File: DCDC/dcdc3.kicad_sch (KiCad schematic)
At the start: 29 parts, among them IC1 LM5145RGYR, J1 Vin, J2 GND, J3 Vout, J4 GND, M1 30V 60A, M2 30V 35A

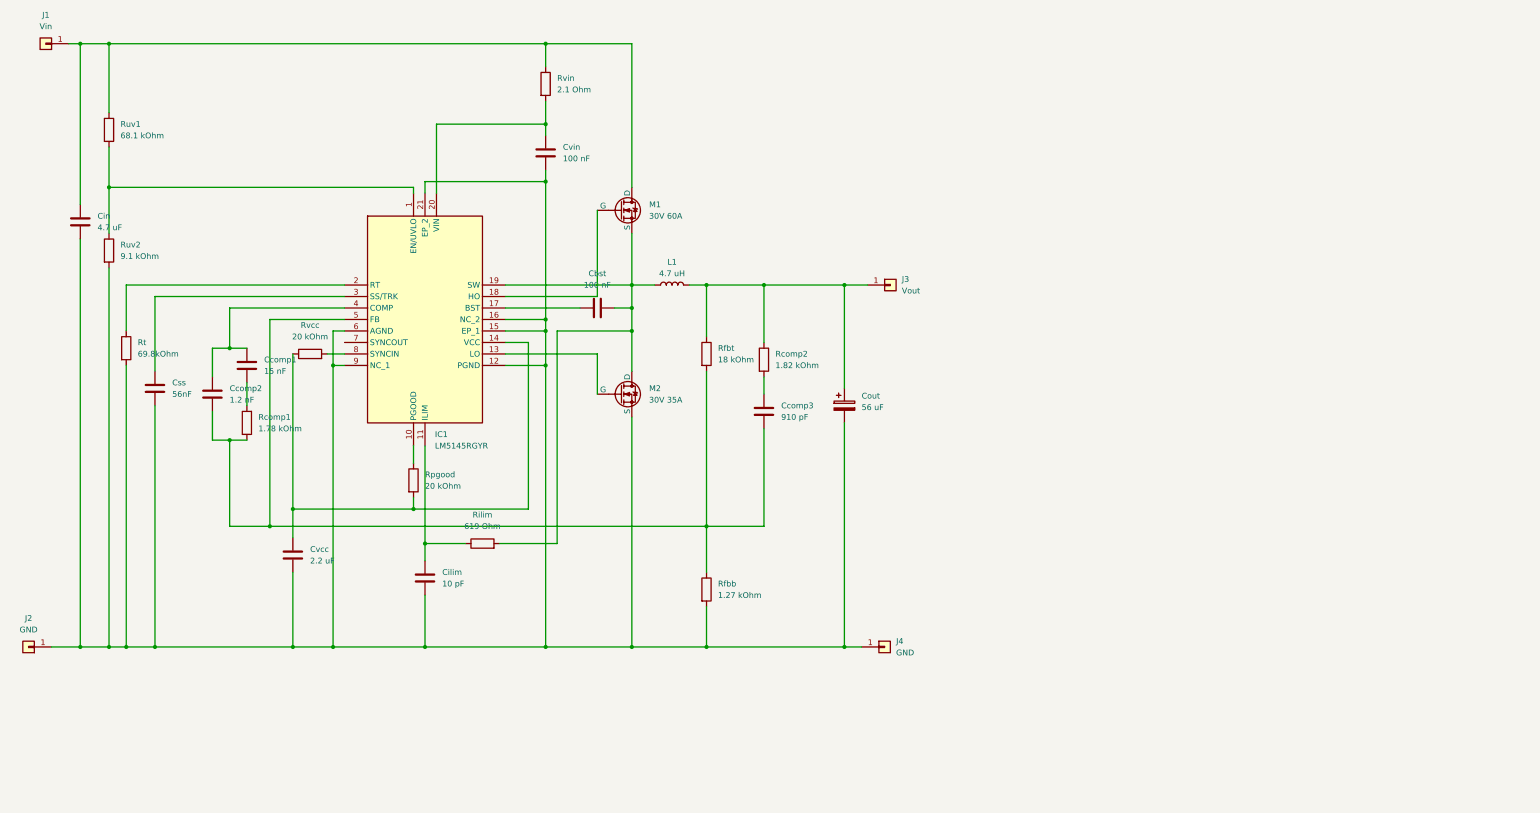
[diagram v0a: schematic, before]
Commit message: redesign of voltage regulator
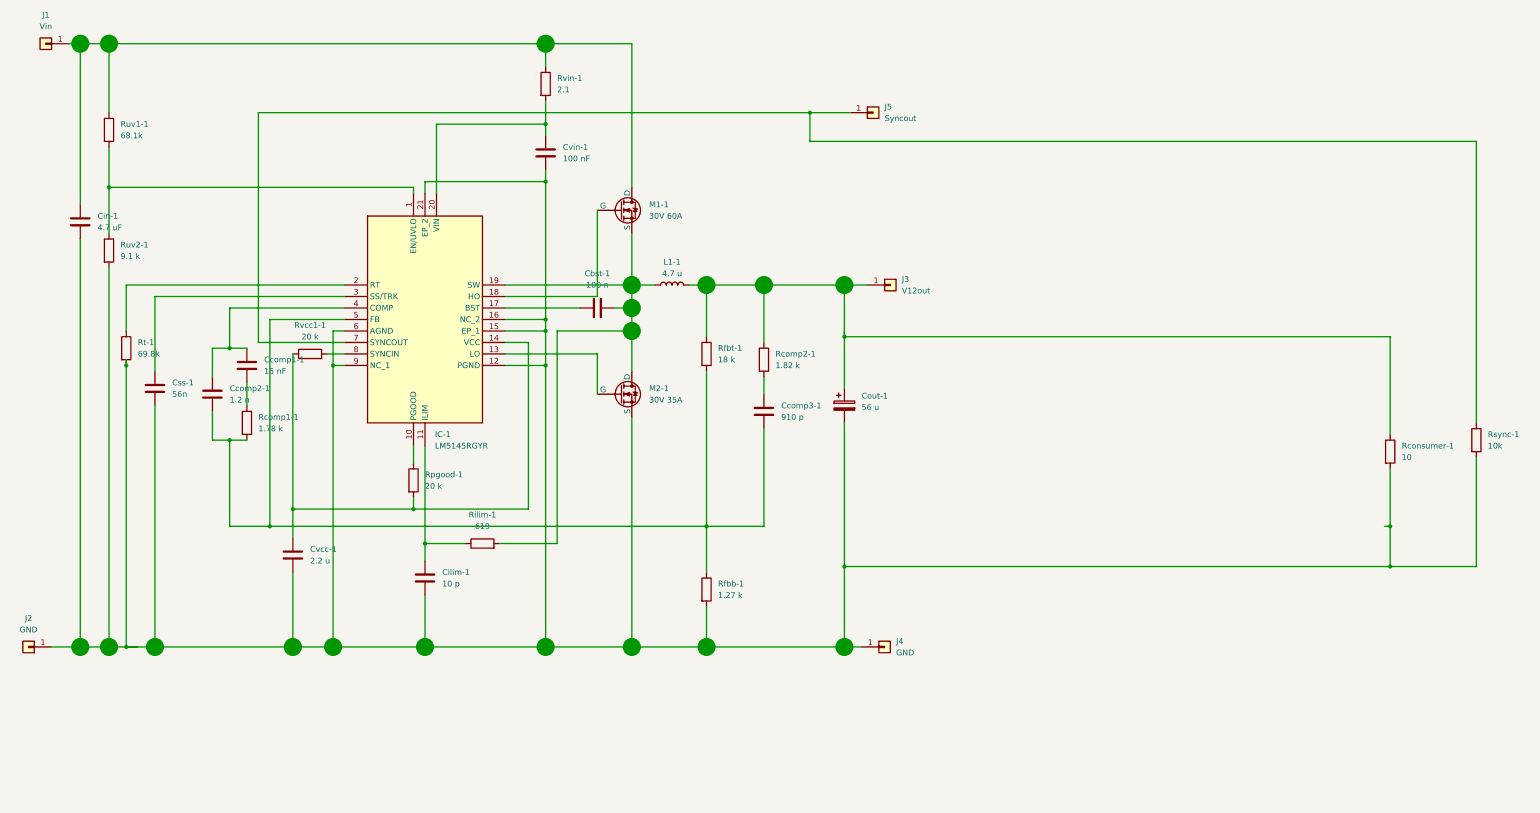
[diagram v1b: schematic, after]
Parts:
- added J5: Syncout, Connector_Pin:Pin_D1.4mm_L8.5mm_W2.8mm_FlatFork, symbol Connector_Generic:Conn_01x01
- added Rconsumer-1: 10, symbol Device:R
- added Rsync-1: 10k, symbol Device:R
- Cbst-1: renamed from Cbst; value 100 nF -> 100 n; footprint (none) -> Capacitor_SMD:C_0603_1608Metric; Manufacturer_Part_Number (none) -> GRM188R61E104KA01D
- Ccomp1-1: renamed from Ccomp1; footprint (none) -> Capacitor_SMD:C_0402_1005Metric; Manufacturer_Part_Number (none) -> GRM155R71C153KA01D
- Ccomp2-1: renamed from Ccomp2; value 1.2 nF -> 1.2 n; footprint (none) -> Capacitor_SMD:C_0402_1005Metric; Manufacturer_Part_Number (none) -> GRM155R71H122KA01D
- Ccomp3-1: renamed from Ccomp3; value 910 pF -> 910 p; footprint (none) -> Capacitor_SMD:C_0402_1005Metric; Manufacturer_Part_Number (none) -> GRM1555C1H911JA01D
- Cilim-1: renamed from Cilim; value 10 pF -> 10 p; footprint (none) -> Capacitor_SMD:C_0603_1608Metric; Manufacturer_Part_Number (none) -> GRM1885C2A100JA01D
- Cin-1: renamed from Cin; footprint (none) -> Capacitor_SMD:C_1210_3225Metric; Manufacturer_Part_Number (none) -> GRM32ER71H475KA88L
- Cout-1: renamed from Cout; value 56 uF -> 56 u; footprint (none) -> Capacitor_THT:C_Radial_D6.3mm_H5.0mm_P2.50mm; Manufacturer_Part_Number (none) -> APSG250ELL560MF05S
- Css-1: renamed from Css; value 56nF -> 56n; footprint (none) -> Capacitor_SMD:C_0402_1005Metric; Manufacturer_Part_Number (none) -> GRM155R71C563KA88D
- Cvcc-1: renamed from Cvcc; value 2.2 uF -> 2.2 u; footprint (none) -> Capacitor_SMD:C_0402_1005Metric; Manufacturer_Part_Number (none) -> C1005X5R1V225K050BC
- Cvin-1: renamed from Cvin; footprint (none) -> Capacitor_SMD:C_0603_1608Metric; Manufacturer_Part_Number (none) -> CGA3E2X7R1H104K080AA
- IC-1: renamed from IC1; footprint RGY0020B -> Library:RGY0020B
- J1, J2, J4: footprint (none) -> Connector_Pin:Pin_D1.4mm_L8.5mm_W2.8mm_FlatFork
- J3: value Vout -> V12out; footprint (none) -> Connector_Pin:Pin_D1.4mm_L8.5mm_W2.8mm_FlatFork
- L1-1: renamed from L1; value 4.7 uH -> 4.7 u; footprint (none) -> Library:A3mmCoil; Manufacturer_Part_Number (none) -> R=15,L=2.145,N=11,d=1.95, Rwire=1.68 mOhm
- M1-1: renamed from M1; footprint (none) -> Library:TO545P521X1594X2566-3P; Manufacturer_Part_Number (none) -> IXFX360N10T
- M2-1: renamed from M2; footprint (none) -> Library:TO545P521X1594X2566-3P; Manufacturer_Part_Number (none) -> IXFX360N10T
- Rcomp1-1: renamed from Rcomp1; value 1.78 kOhm -> 1.78 k; footprint (none) -> Resistor_SMD:R_0402_1005Metric; Manufacturer_Part_Number (none) -> CRCW04021K78FKED
- Rcomp2-1: renamed from Rcomp2; value 1.82 kOhm -> 1.82 k; footprint (none) -> Resistor_SMD:R_0402_1005Metric; Manufacturer_Part_Number (none) -> CRCW04021K82FKED
- Rfbb-1: renamed from Rfbb; value 1.27 kOhm -> 1.27 k; footprint (none) -> Resistor_SMD:R_0402_1005Metric; Manufacturer_Part_Number (none) -> CRCW04021K27FKED
- Rfbt-1: renamed from Rfbt; value 18 kOhm -> 18 k; footprint (none) -> Resistor_SMD:R_0603_1608Metric; Manufacturer_Part_Number (none) -> RC0603FR-0718KL
- Rilim-1: renamed from Rilim; value 619 Ohm -> 619; footprint (none) -> Resistor_SMD:R_0402_1005Metric; Manufacturer_Part_Number (none) -> CRCW0402619RFKED
- Rpgood-1: renamed from Rpgood; value 20 kOhm -> 20 k; footprint (none) -> Resistor_SMD:R_0603_1608Metric; Manufacturer_Part_Number (none) -> RC0603FR-0720KL
- Rt-1: renamed from Rt; value 69.8kOhm -> 69.8k; footprint (none) -> Resistor_SMD:R_0402_1005Metric; Manufacturer_Part_Number (none) -> CRCW040269K8FKED
- Ruv1-1: renamed from Ruv1; value 68.1 kOhm -> 68.1k; footprint (none) -> Resistor_SMD:R_0201_0603Metric; Manufacturer_Part_Number (none) -> RC0201FR-7D68K1L
- Ruv2-1: renamed from Ruv2; value 9.1 kOhm -> 9.1 k; footprint (none) -> Resistor_SMD:R_0603_1608Metric; Manufacturer_Part_Number (none) -> RC0603FR-079K1L
- Rvcc1-1: renamed from Rvcc; value 20 kOhm -> 20 k; footprint (none) -> Resistor_SMD:R_0603_1608Metric; Manufacturer_Part_Number (none) -> RC0603FR-0720KL
- Rvin-1: renamed from Rvin; value 2.1 Ohm -> 2.1; footprint (none) -> Resistor_SMD:R_0603_1608Metric; Manufacturer_Part_Number (none) -> CRCW06032R10FKEA
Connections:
- net at Cilim-1.2, Cin-1.2, Cout-1.2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: now also Rconsumer-1.2, Rsync-1.2
- net at Cout-1.1, J3.1 (Pin_1), L1-1.2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: now also Rconsumer-1.1
- net at IC-1.7 (SYNCOUT): now also J5.1 (Pin_1), Rsync-1.1

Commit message: restructured schematics, dumbed down pcb before redesign
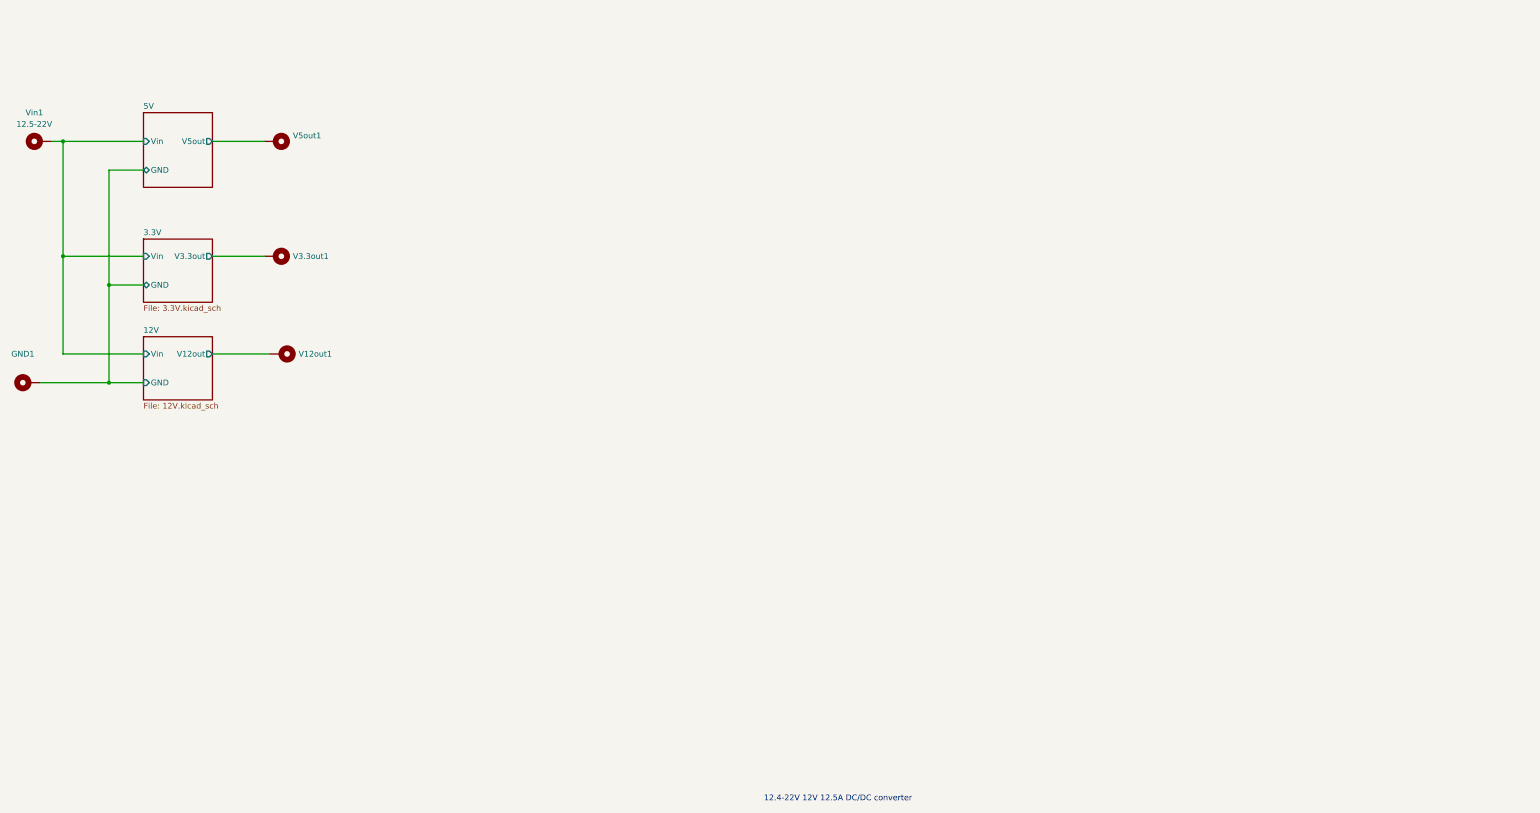
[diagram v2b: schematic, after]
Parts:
- removed Cbst-1: 100 n, Capacitor_SMD:C_0603_1608Metric, symbol Device:C
- removed Ccomp1-1: 15 nF, Capacitor_SMD:C_0402_1005Metric, symbol Device:C
- removed Ccomp2-1: 1.2 n, Capacitor_SMD:C_0402_1005Metric, symbol Device:C
- removed Ccomp3-1: 910 p, Capacitor_SMD:C_0402_1005Metric, symbol Device:C
- removed Cilim-1: 10 p, Capacitor_SMD:C_0603_1608Metric, symbol Device:C
- removed Cin-1: 4.7 uF, Capacitor_SMD:C_1210_3225Metric, symbol Device:C
- removed Cout-1: 56 u, Capacitor_THT:C_Radial_D6.3mm_H5.0mm_P2.50mm, symbol Device:C_Polarized
- removed Css-1: 56n, Capacitor_SMD:C_0402_1005Metric, symbol Device:C
- removed Cvcc-1: 2.2 u, Capacitor_SMD:C_0402_1005Metric, symbol Device:C
- removed Cvin-1: 100 nF, Capacitor_SMD:C_0603_1608Metric, symbol Device:C
- removed IC-1: LM5145RGYR, Library:RGY0020B, symbol New_Library:LM5145RGYR
- removed J1: Vin, Connector_Pin:Pin_D1.4mm_L8.5mm_W2.8mm_FlatFork, symbol Connector_Generic:Conn_01x01
- removed J2, J4: GND, Connector_Pin:Pin_D1.4mm_L8.5mm_W2.8mm_FlatFork, symbol Connector_Generic:Conn_01x01
- removed J3: V12out, Connector_Pin:Pin_D1.4mm_L8.5mm_W2.8mm_FlatFork, symbol Connector_Generic:Conn_01x01
- removed J5: Syncout, Connector_Pin:Pin_D1.4mm_L8.5mm_W2.8mm_FlatFork, symbol Connector_Generic:Conn_01x01
- removed L1-1: 4.7 u, Library:A3mmCoil, symbol Device:L
- removed M1-1: 30V 60A, Library:TO545P521X1594X2566-3P, symbol Simulation_SPICE:NMOS
- removed M2-1: 30V 35A, Library:TO545P521X1594X2566-3P, symbol Simulation_SPICE:NMOS
- removed Rcomp1-1: 1.78 k, Resistor_SMD:R_0402_1005Metric, symbol Device:R
- removed Rcomp2-1: 1.82 k, Resistor_SMD:R_0402_1005Metric, symbol Device:R
- removed Rconsumer-1: 10, symbol Device:R
- removed Rfbb-1: 1.27 k, Resistor_SMD:R_0402_1005Metric, symbol Device:R
- removed Rfbt-1: 18 k, Resistor_SMD:R_0603_1608Metric, symbol Device:R
- removed Rilim-1: 619, Resistor_SMD:R_0402_1005Metric, symbol Device:R
- removed Rpgood-1, Rvcc1-1: 20 k, Resistor_SMD:R_0603_1608Metric, symbol Device:R
- removed Rsync-1: 10k, symbol Device:R
- removed Rt-1: 69.8k, Resistor_SMD:R_0402_1005Metric, symbol Device:R
- removed Ruv1-1: 68.1k, Resistor_SMD:R_0201_0603Metric, symbol Device:R
- removed Ruv2-1: 9.1 k, Resistor_SMD:R_0603_1608Metric, symbol Device:R
- removed Rvin-1: 2.1, Resistor_SMD:R_0603_1608Metric, symbol Device:R
- added GND1: (no value), MountingHole:MountingHole_2.7mm_M2.5_Pad_Via, symbol Mechanical:MountingHole_Pad
- added V12out1, V3.3out1, V5out1: ~, MountingHole:MountingHole_2.7mm_M2.5_Pad_Via, symbol Mechanical:MountingHole_Pad
- added Vin1: 12.5-22V, MountingHole:MountingHole_2.7mm_M2.5_Pad_Via, symbol Mechanical:MountingHole_Pad
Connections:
- new net 12V/GND: GND1.1
- new net 12V/V12out: V12out1.1
- new net 12V/Vin: Vin1.1
- new net 3.3V/V3.3out: V3.3out1.1
- new net 5V/V5out: V5out1.1
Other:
- added sheet 12V (12V.kicad_sch)
- added sheet 3.3V (3.3V.kicad_sch)
- added sheet 5V (5V.kicad_sch)
- note added: "12.4-22V 12V 12.5A DC/DC converter"

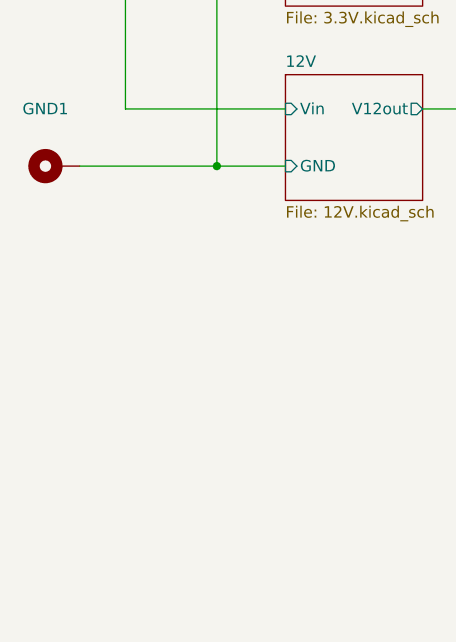
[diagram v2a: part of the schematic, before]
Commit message: pcb updated with all parts
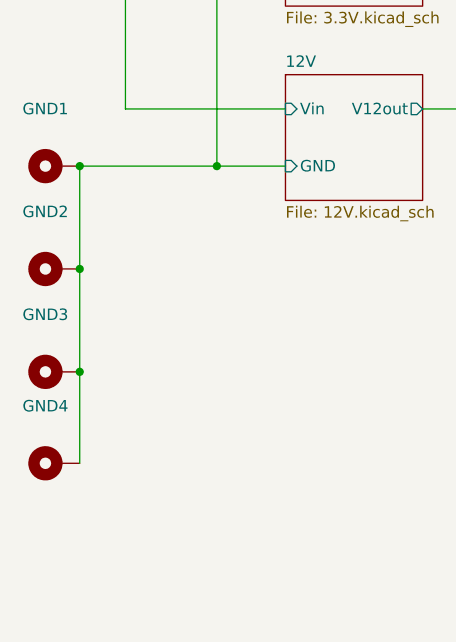
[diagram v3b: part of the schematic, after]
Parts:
- added GND2, GND3, GND4: ~, MountingHole:MountingHole_2.7mm_M2.5_Pad_Via, symbol Mechanical:MountingHole_Pad
- GND1: value (none) -> ~
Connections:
- net 12V/GND: now also GND2.1, GND3.1, GND4.1
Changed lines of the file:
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@@
 (kicad_sch (version 20230121) (generator eeschema)
   (paper "A4")
+  (junction (at 29.21 120.65) (diameter 0) (color 0 0 0 0)
+  )
   (junction (at 44.45 76.2) (diameter 0) (color 0 0 0 0)
   )
+  (junction (at 29.21 97.79) (diameter 0) (color 0 0 0 0)
+  )
   (junction (at 34.29 44.45) (diameter 0) (color 0 0 0 0)
   )
@@
   (junction (at 44.45 97.79) (diameter 0) (color 0 0 0 0)
   )
+  (junction (at 29.21 109.22) (diameter 0) (color 0 0 0 0)
+  )
   (wire (pts (xy 52.07 76.2) (xy 44.45 76.2))
     (stroke (width 0) (type default))
@@
     (stroke (width 0) (type default))
   )
+  (wire (pts (xy 29.21 109.22) (xy 29.21 97.79))
+    (stroke (width 0) (type default))
+  )
   (wire (pts (xy 67.31 69.85) (xy 78.74 69.85))
     (stroke (width 0) (type default))
@@
     (stroke (width 0) (type default))
   )
+  (wire (pts (xy 29.21 109.22) (xy 29.21 120.65))
+    (stroke (width 0) (type default))
+  )
   (wire (pts (xy 34.29 69.85) (xy 34.29 44.45))
     (stroke (width 0) (type default))
@@
   )
   (wire (pts (xy 67.31 91.44) (xy 80.01 91.44))
+    (stroke (width 0) (type default))
+  )
+  (wire (pts (xy 29.21 120.65) (xy 29.21 130.81))
     (stroke (width 0) (type default))
   )
@@
     (effects (font (size 1.27 1.27)) (justify left bottom))
   )
+  (symbol (lib_id "Mechanical:MountingHole_Pad") (at 26.67 130.81 90) (unit 1)
+    (in_bom yes) (on_board yes) (dnp no) (fields_autoplaced)
+    (property "Reference" "GND4" (at 25.4 124.46 90)
+      (effects (font (size 1.27 1.27)))
+    )
+    (property "Value" "~" (at 25.4 127 90)
+      (effects (font (size 1.27 1.27)) hide)
+    )
+    (property "Footprint" "MountingHole:MountingHole_2.7mm_M2.5_Pad_Via" (at 26.67 130.81 0)
+      (effects (font (size 1.27 1.27)) hide)
+    )
+    (property "Datasheet" "~" (at 26.67 130.81 0)
+      (effects (font (size 1.27 1.27)) hide)
+    )
+    (pin "1")
+    (instances
+      (project "dcdc3"
+        (path "/074a9d0b-fc12-4aa8-94e4-356d74449fb4"
+          (reference "GND4") (unit 1)
+        )
+      )
+    )
+  )
   (symbol (lib_id "Mechanical:MountingHole_Pad") (at 81.28 69.85 270) (unit 1)
     (in_bom yes) (on_board yes) (dnp no) (fields_autoplaced)
@@
     )
   )
+  (symbol (lib_id "Mechanical:MountingHole_Pad") (at 26.67 120.65 90) (unit 1)
+    (in_bom yes) (on_board yes) (dnp no) (fields_autoplaced)
+    (property "Reference" "GND3" (at 25.4 114.3 90)
+      (effects (font (size 1.27 1.27)))
+    )
+    (property "Value" "~" (at 25.4 116.84 90)
+      (effects (font (size 1.27 1.27)) hide)
+    )
+    (property "Footprint" "MountingHole:MountingHole_2.7mm_M2.5_Pad_Via" (at 26.67 120.65 0)
+      (effects (font (size 1.27 1.27)) hide)
+    )
+    (property "Datasheet" "~" (at 26.67 120.65 0)
+      (effects (font (size 1.27 1.27)) hide)
+    )
+    (pin "1")
+    (instances
+      (project "dcdc3"
+        (path "/074a9d0b-fc12-4aa8-94e4-356d74449fb4"
+          (reference "GND3") (unit 1)
+        )
+      )
+    )
+  )
   (symbol (lib_id "Mechanical:MountingHole_Pad") (at 82.55 91.44 270) (unit 1)
     (in_bom yes) (on_board yes) (dnp no) (fields_autoplaced)
@@
       (effects (font (size 1.27 1.27)))
     )
-    (property "Value" "" (at 25.4 93.98 90)
+    (property "Value" "~" (at 25.4 93.98 90)
       (effects (font (size 1.27 1.27)) hide)
     )
@@
         )
       )
+    )
+  )
+  (symbol (lib_id "Mechanical:MountingHole_Pad") (at 26.67 109.22 90) (unit 1)
+    (in_bom yes) (on_board yes) (dnp no) (fields_autoplaced)
+    (property "Reference" "GND2" (at 25.4 102.87 90)
+      (effects (font (size 1.27 1.27)))
+    )
+    (property "Value" "~" (at 25.4 105.41 90)
+      (effects (font (size 1.27 1.27)) hide)
+    )
+    (property "Footprint" "MountingHole:MountingHole_2.7mm_M2.5_Pad_Via" (at 26.67 109.22 0)
+      (effects (font (size 1.27 1.27)) hide)
+    )
+    (property "Datasheet" "~" (at 26.67 109.22 0)
+      (effects (font (size 1.27 1.27)) hide)
+    )
+    (pin "1")
+    (instances
+      (project "dcdc3"
+        (path "/074a9d0b-fc12-4aa8-94e4-356d74449fb4"
+          (reference "GND2") (unit 1)
+        )
+      )
